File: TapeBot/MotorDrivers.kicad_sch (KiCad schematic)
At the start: 23 parts, among them J3 43045-0412, J4 43045-0412, J5 43045-0412, J6 43045-0412, J7 43045-0412, J8 43045-0412, J9 43045-0412, U4 TB6612FNG, U5 TB6612FNG, U6 TB6612FNG, U7 TB6612FNG

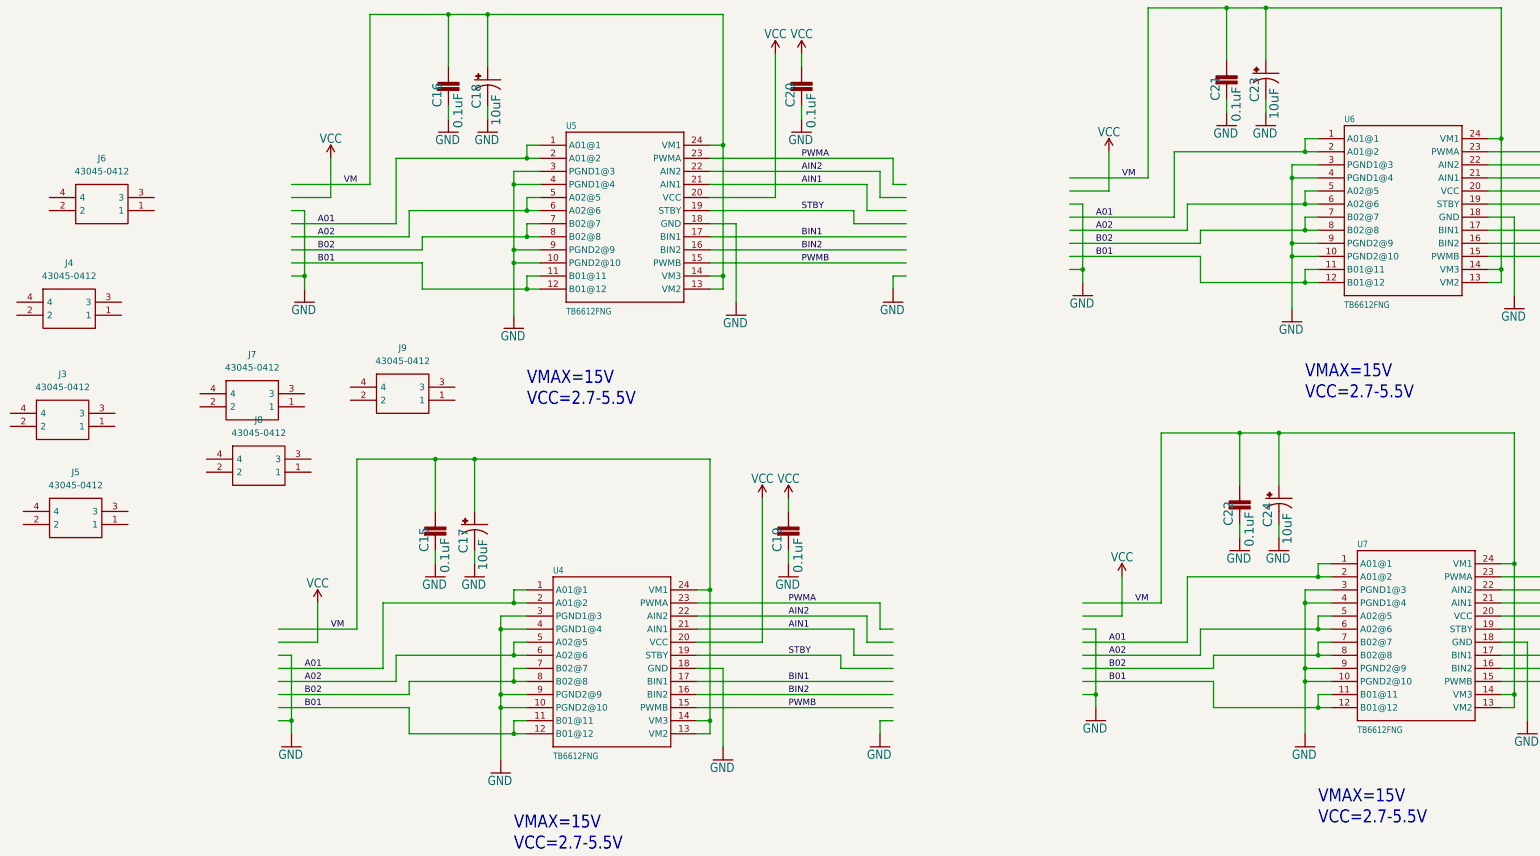
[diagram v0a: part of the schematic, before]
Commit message: fixed footprints and symbols
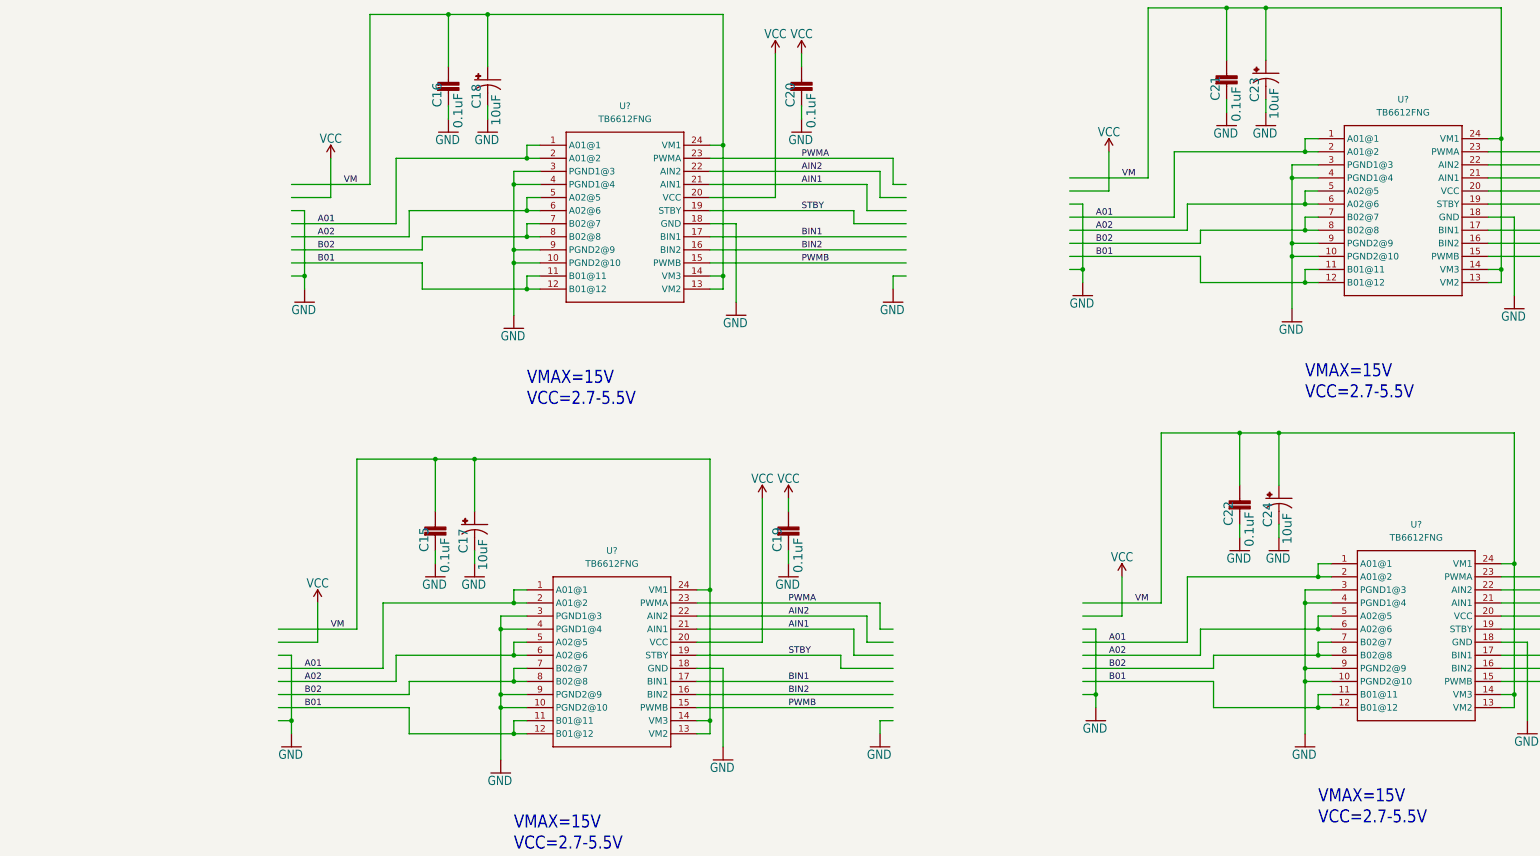
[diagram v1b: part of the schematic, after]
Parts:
- removed J3, J4, J5, J6, J7, J8, J9: 43045-0412, 43045-04(12,13,14), symbol tapebot:43045-0412
- removed U4, U5, U6, U7: TB6612FNG, SparkFun_Motor_Driver-TB6612FNG_v11c:SSOP24, symbol SparkFun_Motor_Driver-TB6612FNG_v11c-eagle-import:TB6612FNG
- added U? (x4): TB6612FNG, tapebot:SOP65P760X160-24N, symbol tapebot:TB6612FNG
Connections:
- net A01: now also U?.1 (A01@1), U?.1 (A01@1), U?.1 (A01@1), U?.1 (A01@1), U?.2 (A01@2), U?.2 (A01@2), U?.2 (A01@2), U?.2 (A01@2)
- net A02: now also U?.5 (A02@5), U?.5 (A02@5), U?.5 (A02@5), U?.5 (A02@5), U?.6 (A02@6), U?.6 (A02@6), U?.6 (A02@6), U?.6 (A02@6)
- net AIN1: now also U?.21 (AIN1), U?.21 (AIN1), U?.21 (AIN1), U?.21 (AIN1)
- net AIN2: now also U?.22 (AIN2), U?.22 (AIN2), U?.22 (AIN2), U?.22 (AIN2)
- net B01: now also U?.11 (B01@11), U?.11 (B01@11), U?.11 (B01@11), U?.11 (B01@11), U?.12 (B01@12), U?.12 (B01@12), U?.12 (B01@12), U?.12 (B01@12)
- net B02: now also U?.7 (B02@7), U?.7 (B02@7), U?.7 (B02@7), U?.7 (B02@7), U?.8 (B02@8), U?.8 (B02@8), U?.8 (B02@8), U?.8 (B02@8)
- net BIN1: now also U?.17 (BIN1), U?.17 (BIN1), U?.17 (BIN1), U?.17 (BIN1)
- net BIN2: now also U?.16 (BIN2), U?.16 (BIN2), U?.16 (BIN2), U?.16 (BIN2)
- net GND: now also U?.10 (PGND2@10), U?.10 (PGND2@10), U?.10 (PGND2@10), U?.10 (PGND2@10), U?.18 (GND), U?.18 (GND), U?.18 (GND), U?.18 (GND), U?.3 (PGND1@3), U?.3 (PGND1@3), U?.3 (PGND1@3), U?.3 (PGND1@3), U?.4 (PGND1@4), U?.4 (PGND1@4), U?.4 (PGND1@4), U?.4 (PGND1@4), U?.9 (PGND2@9), U?.9 (PGND2@9), U?.9 (PGND2@9), U?.9 (PGND2@9)
- net PWMA: now also U?.23 (PWMA), U?.23 (PWMA), U?.23 (PWMA), U?.23 (PWMA)
- net PWMB: now also U?.15 (PWMB), U?.15 (PWMB), U?.15 (PWMB), U?.15 (PWMB)
- net STBY: now also U?.19 (STBY), U?.19 (STBY), U?.19 (STBY), U?.19 (STBY)
- net VCC: now also U?.20 (VCC), U?.20 (VCC), U?.20 (VCC), U?.20 (VCC)
- net VM: now also U?.13 (VM2), U?.13 (VM2), U?.13 (VM2), U?.13 (VM2), U?.14 (VM3), U?.14 (VM3), U?.14 (VM3), U?.14 (VM3), U?.24 (VM1), U?.24 (VM1), U?.24 (VM1), U?.24 (VM1)

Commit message: finished motor driver schematic and load cell schematic
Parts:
- removed C15, C19, C21, C22, C25, C26: 0.1uF, SparkFun_Motor_Driver-TB6612FNG_v11c:0402, symbol SparkFun_Motor_Driver-TB6612FNG_v11c-eagle-import:0.1UF-0402-16V-10%
- removed C17, C23, C24: 10uF, SparkFun_Motor_Driver-TB6612FNG_v11c:EIA3528, symbol SparkFun_Motor_Driver-TB6612FNG_v11c-eagle-import:10UF-POLAR-EIA3528-20V-10%(TA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
- removed U? (x3): TB6612FNG, tapebot:SOP65P760X160-24N, symbol tapebot:TB6612FNG
- added C? (x6): 0.1uF, SparkFun_Motor_Driver-TB6612FNG_v11c:0402, symbol SparkFun_Motor_Driver-TB6612FNG_v11c-eagle-import:0.1UF-0402-16V-10%
- added C? (x3): 10uF, SparkFun_Motor_Driver-TB6612FNG_v11c:EIA3528, symbol SparkFun_Motor_Driver-TB6612FNG_v11c-eagle-import:10UF-POLAR-EIA3528-20V-10%(TA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
- added J? (x8): 9652068, tapebot:9652068, symbol tapebot:9652068
- added U? (x3): TB6612FNG, tapebot:SOP65P760X160-24N, symbol tapebot:TB6612FNG
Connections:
- net VCC is gone; now on net +3.3V: C20.1, U?.20 (VCC)
- net A01: now also J?.3, J?.3, J?.3, J?.3, U?.1 (A01@1), U?.1 (A01@1), U?.1 (A01@1), U?.2 (A01@2), U?.2 (A01@2), U?.2 (A01@2)
- net A02: now also J?.2, J?.2, J?.2, J?.2, U?.5 (A02@5), U?.5 (A02@5), U?.5 (A02@5), U?.6 (A02@6), U?.6 (A02@6), U?.6 (A02@6)
- net B01: now also J?.3, J?.3, J?.3, J?.3, U?.11 (B01@11), U?.11 (B01@11), U?.11 (B01@11), U?.12 (B01@12), U?.12 (B01@12), U?.12 (B01@12)
- net B02: now also J?.2, J?.2, J?.2, J?.2, U?.7 (B02@7), U?.7 (B02@7), U?.7 (B02@7), U?.8 (B02@8), U?.8 (B02@8), U?.8 (B02@8)
- net GND: now also C?.2, C?.2, C?.2, C?.2, C?.2, C?.2, C?.C (-), C?.C (-), C?.C (-), J?.1, J?.1, J?.1, J?.1, J?.1, J?.1, J?.1, J?.1, U?.10 (PGND2@10), U?.10 (PGND2@10), U?.10 (PGND2@10), U?.18 (GND), U?.18 (GND), U?.18 (GND), U?.3 (PGND1@3), U?.3 (PGND1@3), U?.3 (PGND1@3), U?.4 (PGND1@4), U?.4 (PGND1@4), U?.4 (PGND1@4), U?.9 (PGND2@9), U?.9 (PGND2@9), U?.9 (PGND2@9)
- net AIN1 renamed M1_CTL1
- net M1_CTL1: now also U?.21 (AIN1), U?.21 (AIN1), U?.21 (AIN1)
- net AIN2 renamed M1_CTL2
- net M1_CTL2: now also U?.22 (AIN2), U?.22 (AIN2), U?.22 (AIN2)
- net BIN1 renamed M2_CTL1
- net M2_CTL1: now also U?.17 (BIN1), U?.17 (BIN1), U?.17 (BIN1)
- net BIN2 renamed M2_CTL2
- net M2_CTL2: now also U?.16 (BIN2), U?.16 (BIN2), U?.16 (BIN2)
- net PWMA renamed M1_PWM
- net M1_PWM: now also U?.23 (PWMA), U?.23 (PWMA), U?.23 (PWMA)
- net PWMB renamed M2_PWM
- net M2_PWM: now also U?.15 (PWMB), U?.15 (PWMB), U?.15 (PWMB)
- net STBY renamed +3.3V
- net +3.3V: now also C?.1, C?.1, C?.1, J?.6, J?.6, J?.6, J?.6, J?.6, J?.6, J?.6, J?.6, U?.19 (STBY), U?.19 (STBY), U?.19 (STBY), U?.20 (VCC), U?.20 (VCC), U?.20 (VCC)
- net VM renamed +12V
- net +12V: now also C?.1, C?.1, C?.1, C?.A (+), C?.A (+), C?.A (+), U?.13 (VM2), U?.13 (VM2), U?.13 (VM2), U?.14 (VM3), U?.14 (VM3), U?.14 (VM3), U?.24 (VM1), U?.24 (VM1), U?.24 (VM1)
- new net M1_OUT1: J?.5
- new net M1_OUT2: J?.4
- new net M2_OUT1: J?.5
- new net M2_OUT2: J?.4
- new net M3_OUT1: J?.5
- new net M3_OUT2: J?.4
- new net M4_OUT1: J?.5
- new net M4_OUT2: J?.4
- new net M5_OUT1: J?.5
- new net M5_OUT2: J?.4
- new net M6_OUT1: J?.5
- new net M6_OUT2: J?.4
- new net M7_OUT1: J?.5
- new net M7_OUT2: J?.4
- new net M8_OUT1: J?.5
- new net M8_OUT2: J?.4
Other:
- note added: "Motor 1 + Motor 2"
- note added: "Motor 3 + Motor 4"
- note added: "Motor 5 + Motor 6"
- note added: "Motor 7 + Motor 8"
- note added: "Motor Drivers (TB6612FNG)"
- moved on the sheet: C16, C18, C20, U?

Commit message: (mostly) finished schematic
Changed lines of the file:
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@@
-    (stroke (width 0) (type default) (color 0 0 0 0))
-  )
-  (polyline (pts (xy 13.97 204.47) (xy 13.97 15.24))
     (stroke (width 0) (type default) (color 0 0 0 0))
   )
@@
     (stroke (width 0) (type default) (color 0 0 0 0))
   )
-  (polyline (pts (xy 24.13 15.24) (xy 402.59 15.24))
-    (stroke (width 0) (type default) (color 0 0 0 0))
-  )
   (wire (pts (xy 110.49 64.77) (xy 110.49 90.17))
     (stroke (width 0) (type default) (color 0 0 0 0))
@@
     (stroke (width 0) (type default) (color 0 0 0 0))
   )
-  (polyline (pts (xy 13.97 15.24) (xy 24.13 15.24))
-    (stroke (width 0) (type default) (color 0 0 0 0))
-  )
   (wire (pts (xy 173.99 160.02) (xy 173.99 157.48))
     (stroke (width 0) (type default) (color 0 0 0 0))
@@
     (stroke (width 0) (type default) (color 0 0 0 0))
   )
-  (polyline (pts (xy 402.59 204.47) (xy 13.97 204.47))
-    (stroke (width 0) (type default) (color 0 0 0 0))
-  )
   (wire (pts (xy 274.32 163.83) (xy 274.32 176.53))
     (stroke (width 0) (type default) (color 0 0 0 0))
@@
     (stroke (width 0) (type default) (color 0 0 0 0))
   )
-  (polyline (pts (xy 402.59 15.24) (xy 402.59 204.47))
-    (stroke (width 0) (type default) (color 0 0 0 0))
-  )
